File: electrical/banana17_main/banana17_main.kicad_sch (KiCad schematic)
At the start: 24 parts, among them SW1 SW_SPST, U1 RP2040, U2 NCP1117-3.3_SOT223, U3 W25Q128JVS, Y1 ABMB-272-T3

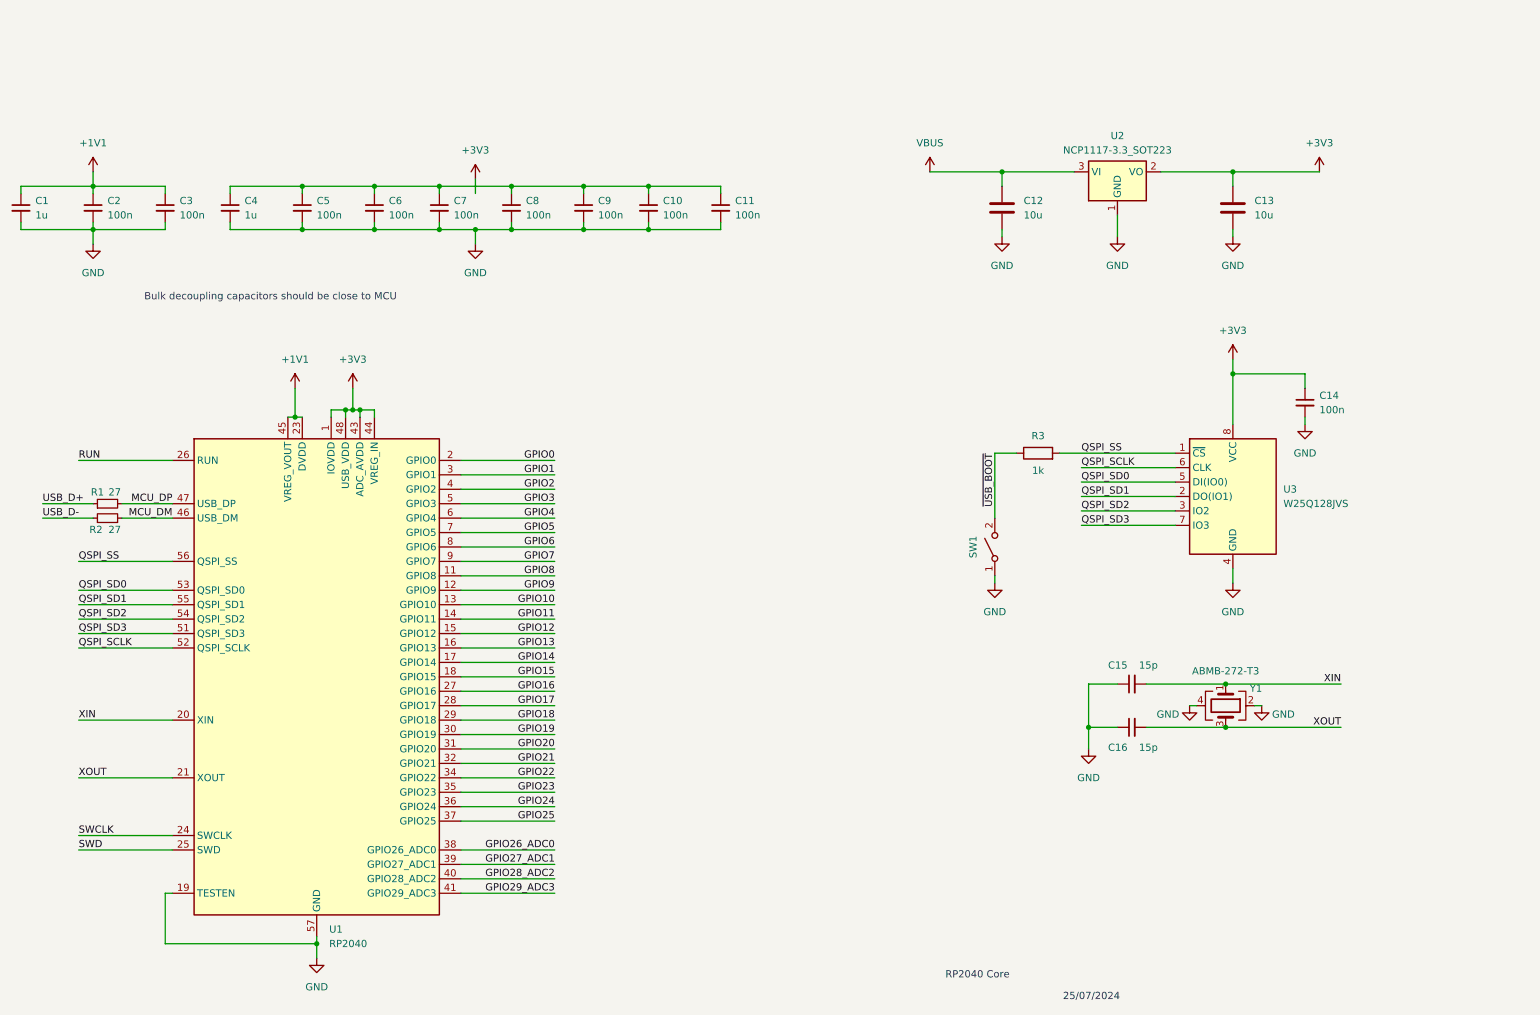
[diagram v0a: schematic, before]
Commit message: RP2040 minimal circuit complete. Pico EZmate connector added for UDB
RP2040 minimal circuit complete. Pico EZmate connector added for UDB.
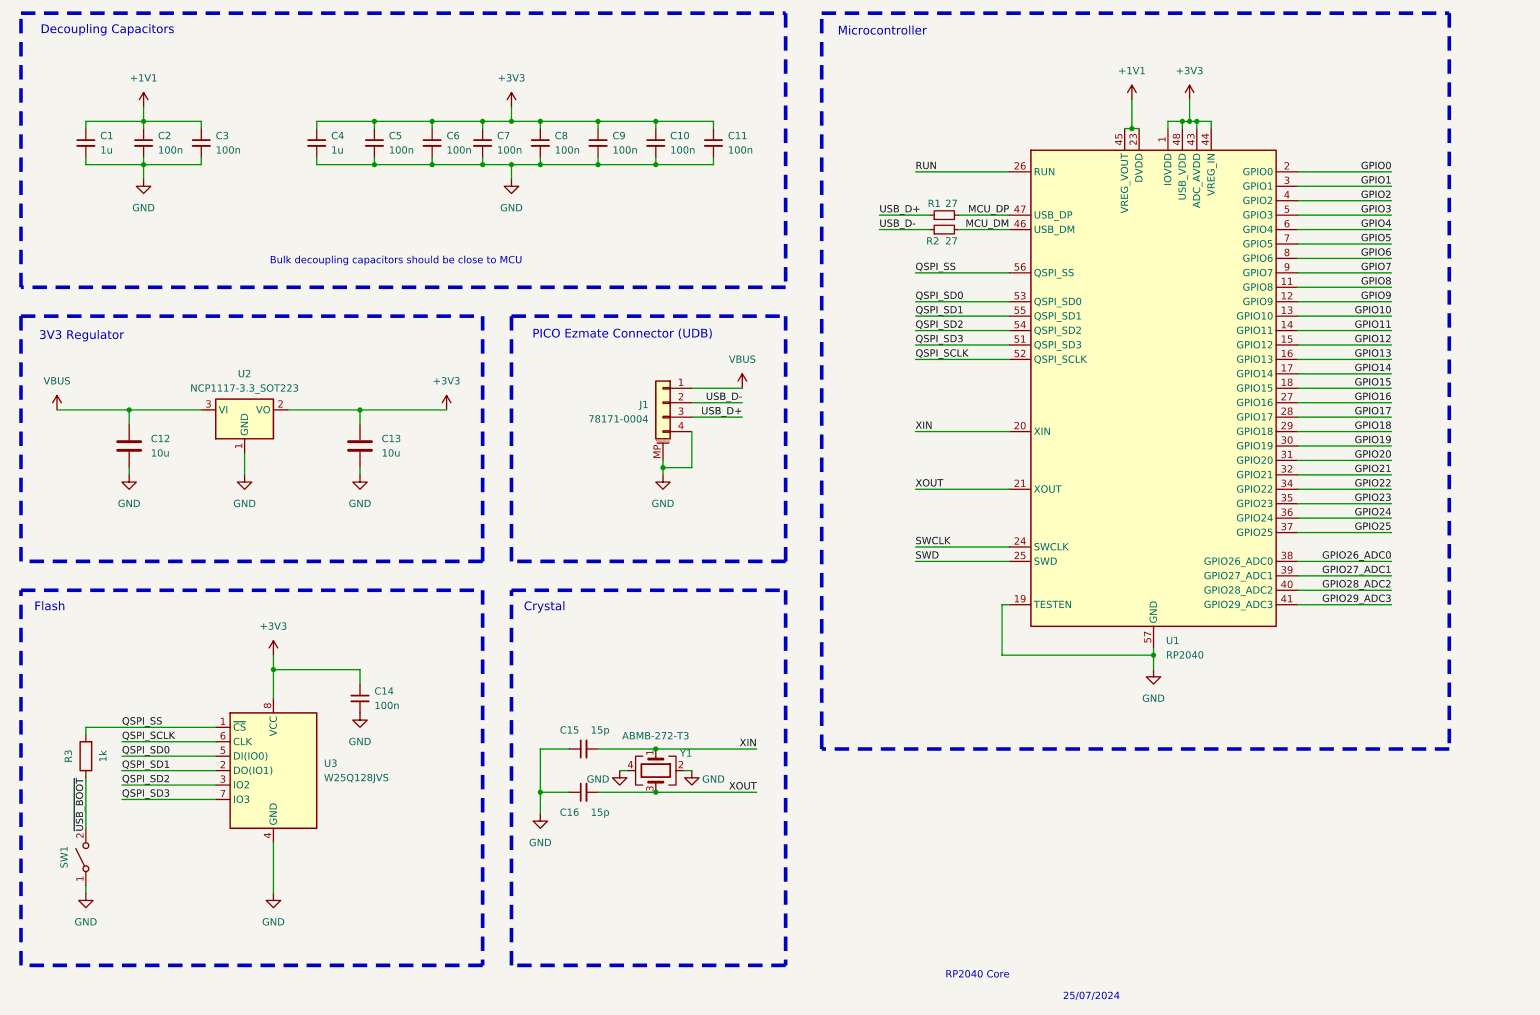
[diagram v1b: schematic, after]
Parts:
- added J1: 78171-0004, symbol Connector_Generic_MountingPin:Conn_01x04_MountingPin
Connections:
- net +3V3: now also C10.1, C11.1, C4.1, C5.1, C6.1, C7.1, C8.1, C9.1
- net GND: now also J1.4 (Pin_4), J1.MP (MountPin)
- net USB_D+: now also J1.3 (Pin_3)
- net USB_D-: now also J1.2 (Pin_2)
- net VBUS: now also J1.1 (Pin_1)
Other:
- note added: "3V3 Regulator"
- note added: "Crystal"
- note added: "Decoupling Capacitors"
- note added: "Flash"
- note added: "Microcontroller"
- note added: "PICO Ezmate Connector (UDB)"
- moved on the sheet: C1, C10, C11, C12, C13, C14, C15, C16, C2, C3, C4, C5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

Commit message: Created child sheet for keyboard matrix.
Created child sheet for keyboard matrix.
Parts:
- renumbered SW1 to BOOT_SEL
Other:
- added sheet Banana17 Matrix (banana17_matrix.kicad_sch)
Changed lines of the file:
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@@
 		(dnp no)
 		(fields_autoplaced yes)
-		(property "Reference" "SW1"
-			(at 31.75 168.91 0)
-			(effects
-				(font
-					(size 1.27 1.27)
-				)
+		(property "Reference" "BOOT_SEL"
+			(at 36.83 168.9099 90)
+			(effects
+				(font
+					(size 1.27 1.27)
+				)
+				(justify right)
 			)
 		)
@@
 			(project "banana17_main"
 				(path "/fd2b462c-d7c2-4bbf-9a41-8b3fef737a65"
-					(reference "SW1")
+					(reference "BOOT_SEL")
 					(unit 1)
 				)
@@
 				)
 			)
+		)
+	)
+	(sheet
+		(at 251.46 156.21)
+		(size 12.7 3.81)
+		(fields_autoplaced yes)
+		(stroke
+			(width 0.1524)
+			(type solid)
+		)
+		(fill
+			(color 0 0 0 0.0000)
+		)
+		(property "Sheetname" "Banana17 Matrix"
+			(at 251.46 155.4984 0)
+			(effects
+				(font
+					(size 1.27 1.27)
+				)
+				(justify left bottom)
+			)
+		)
+		(property "Sheetfile" "banana17_matrix.kicad_sch"
+			(at 251.46 160.6046 0)
+			(effects
+				(font
+					(size 1.27 1.27)
+				)
+				(justify left top)
+			)
+		)
+		(instances
+			(project "banana17_main"
+				(path "/fd2b462c-d7c2-4bbf-9a41-8b3fef737a65"
+					(page "2")
+				)
+			)

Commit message: Altered encoder placement on schematic.
Altered encoder placement on schematic.
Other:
- note added: "Banana 17 Main"
- note removed: "RP2040 Core"
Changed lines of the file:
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@@
 		)
 	)
-	(text "RP2040 Core"
+	(text "Banana 17 Main"
 		(exclude_from_sim no)
-		(at 192.532 189.738 0)
+		(at 194.056 189.738 0)
 		(effects
 			(font
@@
 	)
 	(sheet
-		(at 251.46 156.21)
+		(at 176.53 156.21)
 		(size 12.7 3.81)
 		(fields_autoplaced yes)
@@
 		)
 		(property "Sheetname" "Banana17 Matrix"
-			(at 251.46 155.4984 0)
+			(at 176.53 155.4984 0)
 			(effects
 				(font
@@
 		)
 		(property "Sheetfile" "banana17_matrix.kicad_sch"
-			(at 251.46 160.6046 0)
+			(at 176.53 160.6046 0)
 			(effects
 				(font

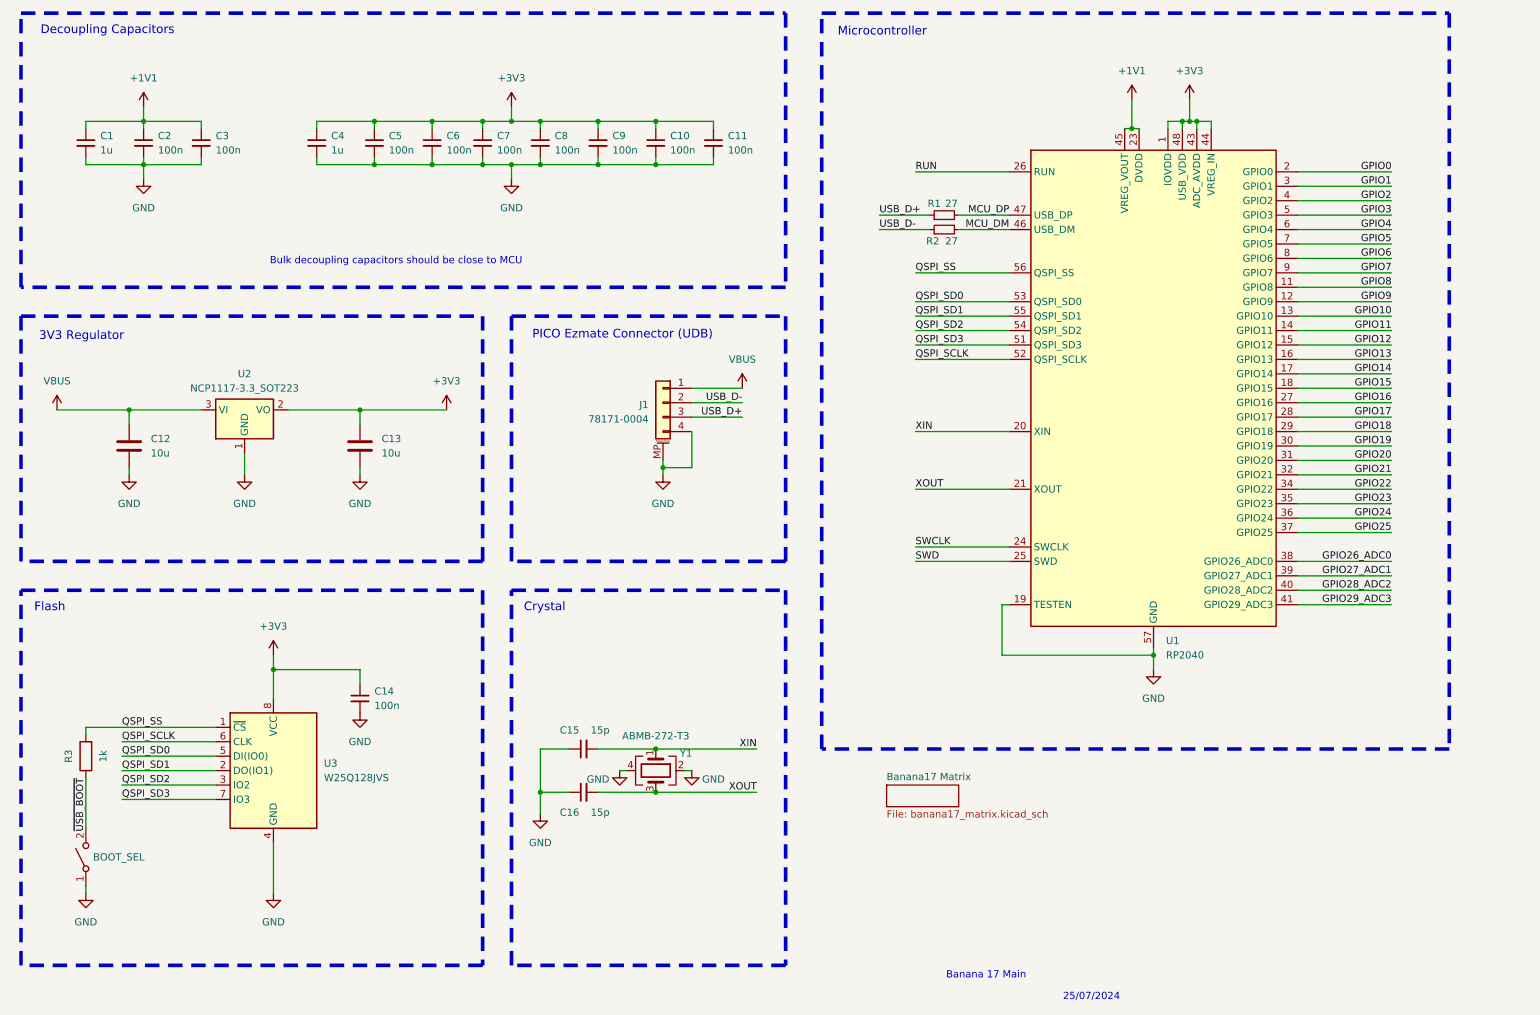
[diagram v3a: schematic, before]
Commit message: SSD1306 symbol and footprint completed and wired up.
SSD1306 symbol and footprint completed and wired up.
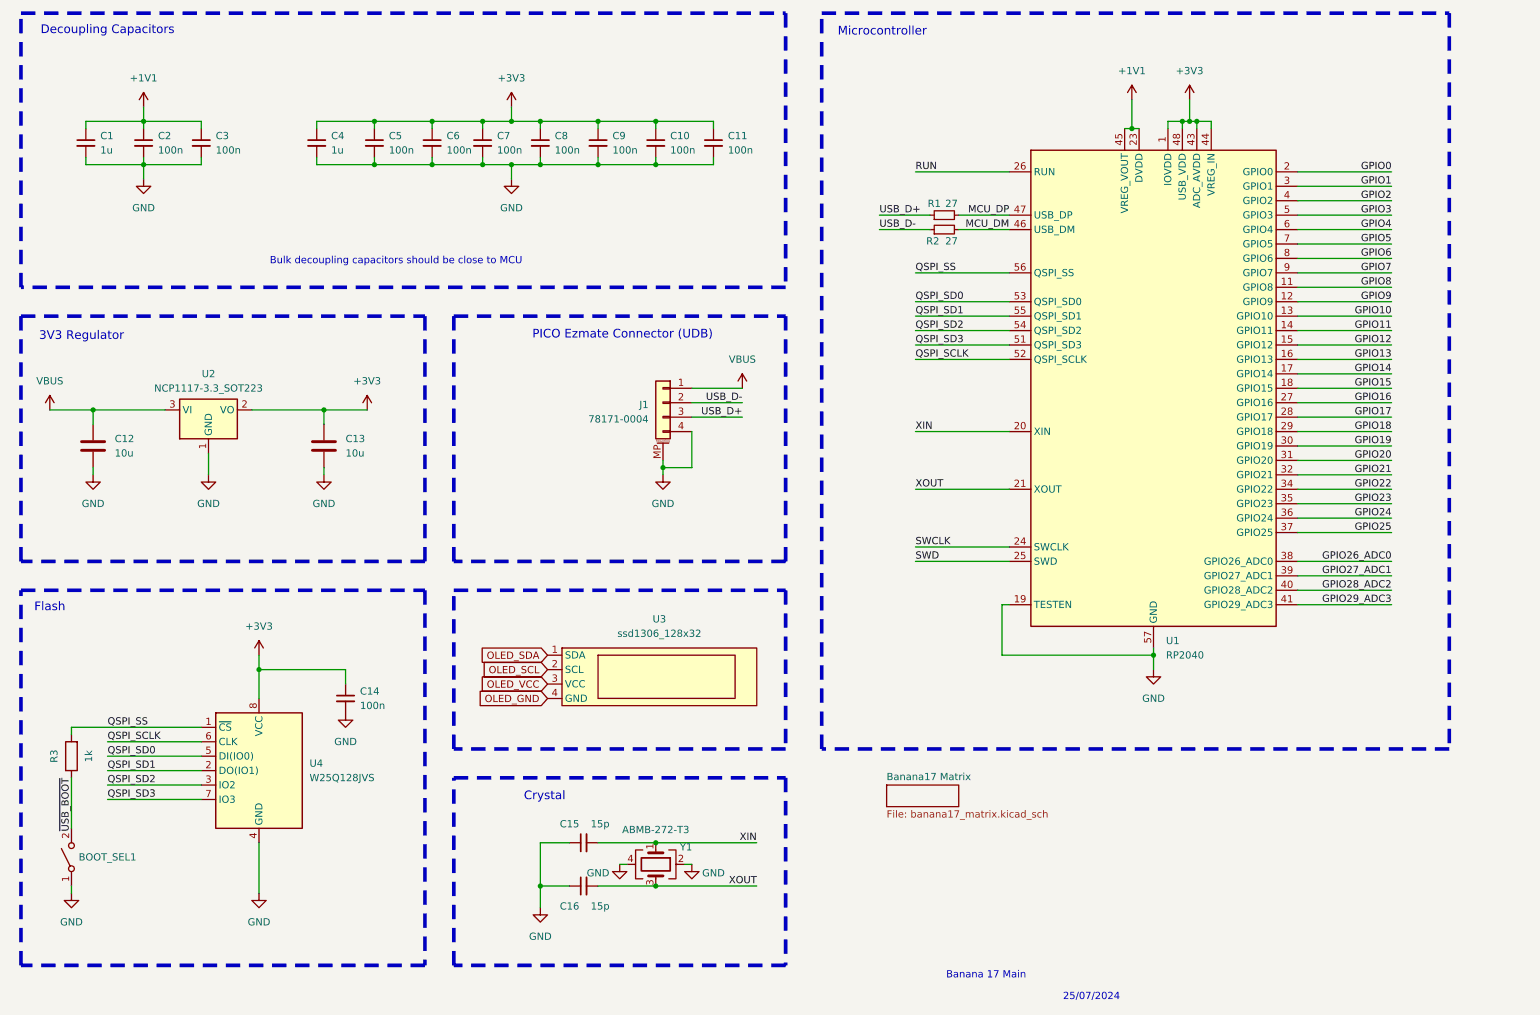
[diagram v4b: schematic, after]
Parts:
- added U3: ssd1306_128x32, Display_GKC:ssd1306_128x32, symbol Display_GKC:ssd1306_128x32
- renumbered BOOT_SEL to BOOT_SEL1, U3 to U4
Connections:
- new net OLED_GND: U3.4 (GND)
- new net OLED_SCL: U3.2 (SCL)
- new net OLED_SDA: U3.1 (SDA)
- new net OLED_VCC: U3.3 (VCC)
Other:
- moved on the sheet: BOOT_SEL1, C12, C13, C14, C15, C16, R3, U2, U4, Y1

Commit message: Initial footprint all selected. Schematic capture complete.
Initial footprint all selected. Schematic capture complete.
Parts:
- BOOT_SEL1: footprint (none) -> Button_Switch_SMD:SW_SPST_TL3305A
- C1, C10, C11, C12, C13, C14, C15, C16, C2, C3, C4, C5, C6, C7, C8, C9: footprint (none) -> Capacitor_SMD:C_0805_2012Metric_Pad1.18x1.45mm_HandSolder
- J1: footprint (none) -> Connector_Molex:Molex_Pico-EZmate_78171-0004_1x04-1MP_P1.20mm_Vertical
- R1, R2, R3: footprint (none) -> Resistor_SMD:R_0805_2012Metric_Pad1.20x1.40mm_HandSolder
- Y1: footprint (none) -> Crystal:Crystal_SMD_Abracon_ABM8G-4Pin_3.2x2.5mm
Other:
- note added: "OLED"
- moved on the sheet: C12, C13, C15, C16, J1, U2, Y1
